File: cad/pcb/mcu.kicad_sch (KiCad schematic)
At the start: 34 parts, among them X4 SWD-Conn, X5 UART_Conn, Y1 32MHz, Y2 32.768k

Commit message: add pcb layout
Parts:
- removed AE1: Antenna_Chip, myLib:Ignion_NN01-102_BT_WIFI, symbol Device:Antenna_Chip
- removed TP10: TXD, TestPoint:TestPoint_Pad_D1.0mm, symbol Connector:TestPoint
- removed TP11: RXD, TestPoint:TestPoint_Pad_D1.0mm, symbol Connector:TestPoint
- removed V6: nRF52810-QFxx, Package_DFN_QFN:QFN-48-1EP_6x6mm_P0.4mm_EP4.6x4.6mm, symbol MCU_Nordic:nRF52810-QFxx
- added AE1: Antenna_Chip, myLib:Ignion_NN01-102_BT_WIFI, symbol Device:Antenna
- added V6: nRF52810-QCxx, Package_DFN_QFN:QFN-32-1EP_5x5mm_P0.5mm_EP3.6x3.6mm, symbol MCU_Nordic:nRF52810-QCxx
- S1: footprint Button_Switch_SMD:SW_SPST_CK_RS282G05A3 -> myLib:Tactile_E-Switch_TL3780AF240QG
- S2, S3: footprint Button_Switch_SMD:SW_SPST_CK_RS282G05A3 -> myLib:Tactile_Panasonic_EVQ-P7J01P
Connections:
- net +3.3V: now also V6.25 (VDD), V6.32 (VDD), V6.9 (VDD)
- net BAT_SENS: now also V6.27 (P0.28/AIN4)
- net BTN0: now also V6.15 (P0.20)
- net BTN1: now also V6.26 (P0.25)
- net CS_IO: now also V6.10 (P0.12)
- net DBG_LED: now also V6.14 (P0.18)
- net DCC: now also V6.31 (DCC)
- net DEC1: now also V6.1 (DEC1)
- net DEC3: now also V6.22 (DEC3)
- net DEC4: now also V6.30 (DEC4)
- net GND: now also V6.20 (VSS), V6.29 (VSS), V6.33 (VSS)
- net GYRO_INT: now also V6.6 (P0.06)
- net HSE1: now also V6.23 (XC1)
- net HSE2: now also V6.24 (XC2)
- net LSE1: now also V6.2 (P0.00/XL1)
- net LSE2: now also V6.3 (P0.01/XL2)
- net MISO: now also V6.13 (P0.16)
- net MOSI: now also V6.11 (P0.14)
- net NRST: now also V6.16 (P0.21/~{RESET})
- net PHOTO: now also V6.28 (P0.30/AIN6)
- net RXD: now also V6.8 (P0.10)
- net SCK: now also V6.12 (P0.15)
- net SCL: now also V6.4 (P0.04/AIN2)
- net SDA: now also V6.5 (P0.05/AIN3)
- net SWDCLK: now also V6.17 (SWDCLK)
- net SWDIO: now also V6.18 (SWDIO)
- net TXD: now also V6.7 (P0.09)
- net ANT_IN: now reaches C17.1, L5.2
- net ANT_IN: now also V6.19 (ANT)
- net RF renamed ANT_TP
- net ANT_TP: now also AE1.1 (A)
- no-connect marks 20 -> 4
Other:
- note removed: "CTS"
- note removed: "RTS"
- moved on the sheet: C14, C8, C9, L3, L4

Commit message: add power section on pcb layout
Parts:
- renumbered C11 to C10, C12 to C11, C13 to C12, C8 to C13, C15 to C14, C9 to C15, C14 to C16, C16 to C17, C17 to C18, C18 to C19, C10 to C9
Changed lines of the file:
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@@
   (symbol (lib_id "power:GND") (at 38.1 190.5 0) (unit 1)
     (in_bom yes) (on_board yes)
-    (property "Reference" "#PWR048" (id 0) (at 38.1 196.85 0)
+    (property "Reference" "#PWR050" (id 0) (at 38.1 196.85 0)
       (effects (font (size 1.27 1.27)) hide)
     )
@@
   (symbol (lib_id "Device:C_Small") (at 101.6 39.37 0) (unit 1)
     (in_bom yes) (on_board yes)
-    (property "Reference" "C11" (id 0) (at 96.52 39.37 0)
+    (property "Reference" "C10" (id 0) (at 96.52 39.37 0)
       (effects (font (size 1.27 1.27)) (justify left))
     )
@@
   (symbol (lib_id "power:GND") (at 233.68 116.84 0) (unit 1)
     (in_bom yes) (on_board yes)
-    (property "Reference" "#PWR041" (id 0) (at 233.68 123.19 0)
+    (property "Reference" "#PWR043" (id 0) (at 233.68 123.19 0)
       (effects (font (size 1.27 1.27)) hide)
     )
@@
   (symbol (lib_id "power:+3.3V") (at 82.55 68.58 0) (unit 1)
     (in_bom yes) (on_board yes)
-    (property "Reference" "#PWR031" (id 0) (at 82.55 72.39 0)
+    (property "Reference" "#PWR037" (id 0) (at 82.55 72.39 0)
       (effects (font (size 1.27 1.27)) hide)
     )
@@
   (symbol (lib_id "power:+3.3V") (at 116.84 33.02 0) (unit 1)
     (in_bom yes) (on_board yes)
-    (property "Reference" "#PWR028" (id 0) (at 116.84 36.83 0)
+    (property "Reference" "#PWR030" (id 0) (at 116.84 36.83 0)
       (effects (font (size 1.27 1.27)) hide)
     )
@@
   (symbol (lib_id "power:+3.3V") (at 130.81 166.37 0) (unit 1)
     (in_bom yes) (on_board yes)
-    (property "Reference" "#PWR046" (id 0) (at 130.81 170.18 0)
+    (property "Reference" "#PWR048" (id 0) (at 130.81 170.18 0)
       (effects (font (size 1.27 1.27)) hide)
     )
@@
   (symbol (lib_id "power:+3.3V") (at 257.81 25.4 0) (unit 1)
     (in_bom yes) (on_board yes)
-    (property "Reference" "#PWR027" (id 0) (at 257.81 29.21 0)
+    (property "Reference" "#PWR029" (id 0) (at 257.81 29.21 0)
       (effects (font (size 1.27 1.27)) hide)
     )
@@
   (symbol (lib_id "power:GND") (at 57.15 68.58 0) (unit 1)
     (in_bom yes) (on_board yes)
-    (property "Reference" "#PWR030" (id 0) (at 57.15 74.93 0)
+    (property "Reference" "#PWR036" (id 0) (at 57.15 74.93 0)
       (effects (font (size 1.27 1.27)) hide)
     )
@@
   (symbol (lib_id "power:GND") (at 233.68 91.44 0) (unit 1)
     (in_bom yes) (on_board yes)
-    (property "Reference" "#PWR038" (id 0) (at 233.68 97.79 0)
+    (property "Reference" "#PWR040" (id 0) (at 233.68 97.79 0)
       (effects (font (size 1.27 1.27)) hide)
     )
@@
   (symbol (lib_id "Device:C_Small") (at 62.23 48.26 270) (unit 1)
     (in_bom yes) (on_board yes)
-    (property "Reference" "C8" (id 0) (at 60.3119 51.0586 90)
+    (property "Reference" "C13" (id 0) (at 60.3119 51.0586 90)
       (effects (font (size 1.27 1.27)) (justify left))
     )
@@
   (symbol (lib_id "Device:C_Small") (at 116.84 39.37 0) (unit 1)
     (in_bom yes) (on_board yes)
-    (property "Reference" "C13" (id 0) (at 111.3214 39.3699 0)
+    (property "Reference" "C12" (id 0) (at 111.3214 39.3699 0)
       (effects (font (size 1.27 1.27)) (justify left))
     )
@@
   (symbol (lib_id "power:GND") (at 130.81 181.61 0) (unit 1)
     (in_bom yes) (on_board yes)
-    (property "Reference" "#PWR047" (id 0) (at 130.81 187.96 0)
+    (property "Reference" "#PWR049" (id 0) (at 130.81 187.96 0)
       (effects (font (size 1.27 1.27)) hide)
     )
@@
   (symbol (lib_id "power:GND") (at 54.61 86.36 0) (unit 1)
     (in_bom yes) (on_board yes)
-    (property "Reference" "#PWR037" (id 0) (at 54.61 92.71 0)
+    (property "Reference" "#PWR039" (id 0) (at 54.61 92.71 0)
       (effects (font (size 1.27 1.27)) hide)
     )
@@
   (symbol (lib_id "Device:C_Small") (at 194.31 38.1 270) (mirror x) (unit 1)
     (in_bom yes) (on_board yes)
-    (property "Reference" "C10" (id 0) (at 194.3257 41.055 90))
+    (property "Reference" "C9" (id 0) (at 194.3257 41.055 90))
     (property "Value" "12p" (id 1) (at 194.2453 42.8228 90))
     (property "Footprint" "Capacitor_SMD:C_0603_1608Metric" (id 2) (at 194.31 38.1 0)
@@
   (symbol (lib_id "power:GND") (at 116.84 45.72 0) (unit 1)
     (in_bom yes) (on_board yes)
-    (property "Reference" "#PWR029" (id 0) (at 116.84 52.07 0)
+    (property "Reference" "#PWR031" (id 0) (at 116.84 52.07 0)
       (effects (font (size 1.27 1.27)) hide)
     )
@@
   (symbol (lib_id "power:+3.3V") (at 40.64 152.4 0) (unit 1)
     (in_bom yes) (on_board yes)
-    (property "Reference" "#PWR045" (id 0) (at 40.64 156.21 0)
+    (property "Reference" "#PWR047" (id 0) (at 40.64 156.21 0)
       (effects (font (size 1.27 1.27)) hide)
     )
@@
   (symbol (lib_id "Device:C_Small") (at 109.22 39.37 0) (unit 1)
     (in_bom yes) (on_board yes)
-    (property "Reference" "C12" (id 0) (at 104.14 39.37 0)
+    (property "Reference" "C11" (id 0) (at 104.14 39.37 0)
       (effects (font (size 1.27 1.27)) (justify left))
     )
@@
   (symbol (lib_id "power:+3.3V") (at 251.46 77.47 0) (unit 1)
     (in_bom yes) (on_board yes)
-    (property "Reference" "#PWR036" (id 0) (at 251.46 81.28 0)
+    (property "Reference" "#PWR038" (id 0) (at 251.46 81.28 0)
       (effects (font (size 1.27 1.27)) hide)
     )
@@
   (symbol (lib_id "Device:C_Small") (at 62.23 55.88 270) (unit 1)
     (in_bom yes) (on_board yes)
-    (property "Reference" "C9" (id 0) (at 60.277 58.6466 90)
+    (property "Reference" "C15" (id 0) (at 60.277 58.6466 90)
       (effects (font (size 1.27 1.27)) (justify left))
     )
@@
   (symbol (lib_id "Device:C_Small") (at 194.31 88.9 270) (mirror x) (unit 1)
     (in_bom yes) (on_board yes)
-    (property "Reference" "C18" (id 0) (at 194.4037 91.681 90))
+    (property "Reference" "C19" (id 0) (at 194.4037 91.681 90))
     (property "Value" "12p" (id 1) (at 194.2832 93.4889 90))
     (property "Footprint" "Capacitor_SMD:C_0603_1608Metric" (id 2) (at 194.31 88.9 0)
@@
   (symbol (lib_id "Device:C_Small") (at 62.23 63.5 270) (unit 1)
     (in_bom yes) (on_board yes)
-    (property "Reference" "C14" (id 0) (at 60.277 66.5142 90)
+    (property "Reference" "C16" (id 0) (at 60.277 66.5142 90)
       (effects (font (size 1.27 1.27)) (justify left))
     )
@@
   (symbol (lib_id "power:+3.3V") (at 251.46 128.27 0) (unit 1)
     (in_bom yes) (on_board yes)
-    (property "Reference" "#PWR042" (id 0) (at 251.46 132.08 0)
+    (property "Reference" "#PWR045" (id 0) (at 251.46 132.08 0)
       (effects (font (size 1.27 1.27)) hide)
     )
@@
   (symbol (lib_id "Device:C_Small") (at 194.31 50.8 270) (mirror x) (unit 1)
     (in_bom yes) (on_board yes)
-    (property "Reference" "C15" (id 0) (at 194.4037 53.581 90))
+    (property "Reference" "C14" (id 0) (at 194.4037 53.581 90))
     (property "Value" "12p" (id 1) (at 194.2832 55.3889 90))
     (property "Footprint" "Capacitor_SMD:C_0603_1608Metric" (id 2) (at 194.31 50.8 0)
@@
   (symbol (lib_id "power:GND") (at 203.2 92.71 0) (mirror y) (unit 1)
     (in_bom yes) (on_board yes)
-    (property "Reference" "#PWR039" (id 0) (at 203.2 99.06 0)
+    (property "Reference" "#PWR041" (id 0) (at 203.2 99.06 0)
       (effects (font (size 1.27 1.27)) hide)
     )
@@
   (symbol (lib_id "Device:C_Small") (at 194.31 76.2 270) (mirror x) (unit 1)
     (in_bom yes) (on_board yes)
-    (property "Reference" "C16" (id 0) (at 194.3257 79.155 90))
+    (property "Reference" "C17" (id 0) (at 194.3257 79.155 90))
     (property "Value" "12p" (id 1) (at 194.2453 80.9228 90))
     (property "Footprint" "Capacitor_SMD:C_0603_1608Metric" (id 2) (at 194.31 76.2 0)
@@
   (symbol (lib_id "Device:C_Small") (at 54.61 82.55 0) (unit 1)
     (in_bom yes) (on_board yes)
-    (property "Reference" "C17" (id 0) (at 48.9952 82.5703 0)
+    (property "Reference" "C18" (id 0) (at 48.9952 82.5703 0)
       (effects (font (size 1.27 1.27)) (justify left))
     )
@@
   (symbol (lib_id "power:GND") (at 177.8 139.7 0) (unit 1)
     (in_bom yes) (on_board yes)
-    (property "Reference" "#PWR043" (id 0) (at 177.8 146.05 0)
+    (property "Reference" "#PWR046" (id 0) (at 177.8 146.05 0)
       (effects (font (size 1.27 1.27)) hide)
     )
@@
   (symbol (lib_id "power:+3.3V") (at 251.46 102.87 0) (unit 1)
     (in_bom yes) (on_board yes)
-    (property "Reference" "#PWR040" (id 0) (at 251.46 106.68 0)
+    (property "Reference" "#PWR042" (id 0) (at 251.46 106.68 0)
       (effects (font (size 1.27 1.27)) hide)
     )
@@
   (symbol (lib_id "power:+3.3V") (at 245.11 25.4 0) (unit 1)
     (in_bom yes) (on_board yes)
-    (property "Reference" "#PWR026" (id 0) (at 245.11 29.21 0)
-      (effects (font (size 1.27 1.27)) hide)
-    )
+    (property "Reference" "#PWR028" (id 0) (at 245.11 29.21 0)
+      (effects (font (size 1.27 1.27)) hide)
+    )

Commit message: add back layer led-ring
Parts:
- S2, S3: footprint myLib:Tactile_Panasonic_EVQ-P7J01P -> myLib:Tactile_Panasonic_EVQP7J01P
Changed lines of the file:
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@@
     (property "Reference" "S2" (id 0) (at 242.57 92.71 0))
     (property "Value" "BTN0" (id 1) (at 242.57 95.25 0))
-    (property "Footprint" "myLib:Tactile_Panasonic_EVQ-P7J01P" (id 2) (at 242.57 88.9 0)
+    (property "Footprint" "myLib:Tactile_Panasonic_EVQP7J01P" (id 2) (at 242.57 88.9 0)
       (effects (font (size 1.27 1.27)) hide)
     )
@@
     (property "Reference" "S3" (id 0) (at 242.57 118.11 0))
     (property "Value" "BTN1" (id 1) (at 242.57 120.65 0))
-    (property "Footprint" "myLib:Tactile_Panasonic_EVQ-P7J01P" (id 2) (at 242.57 114.3 0)
+    (property "Footprint" "myLib:Tactile_Panasonic_EVQP7J01P" (id 2) (at 242.57 114.3 0)
       (effects (font (size 1.27 1.27)) hide)
     )

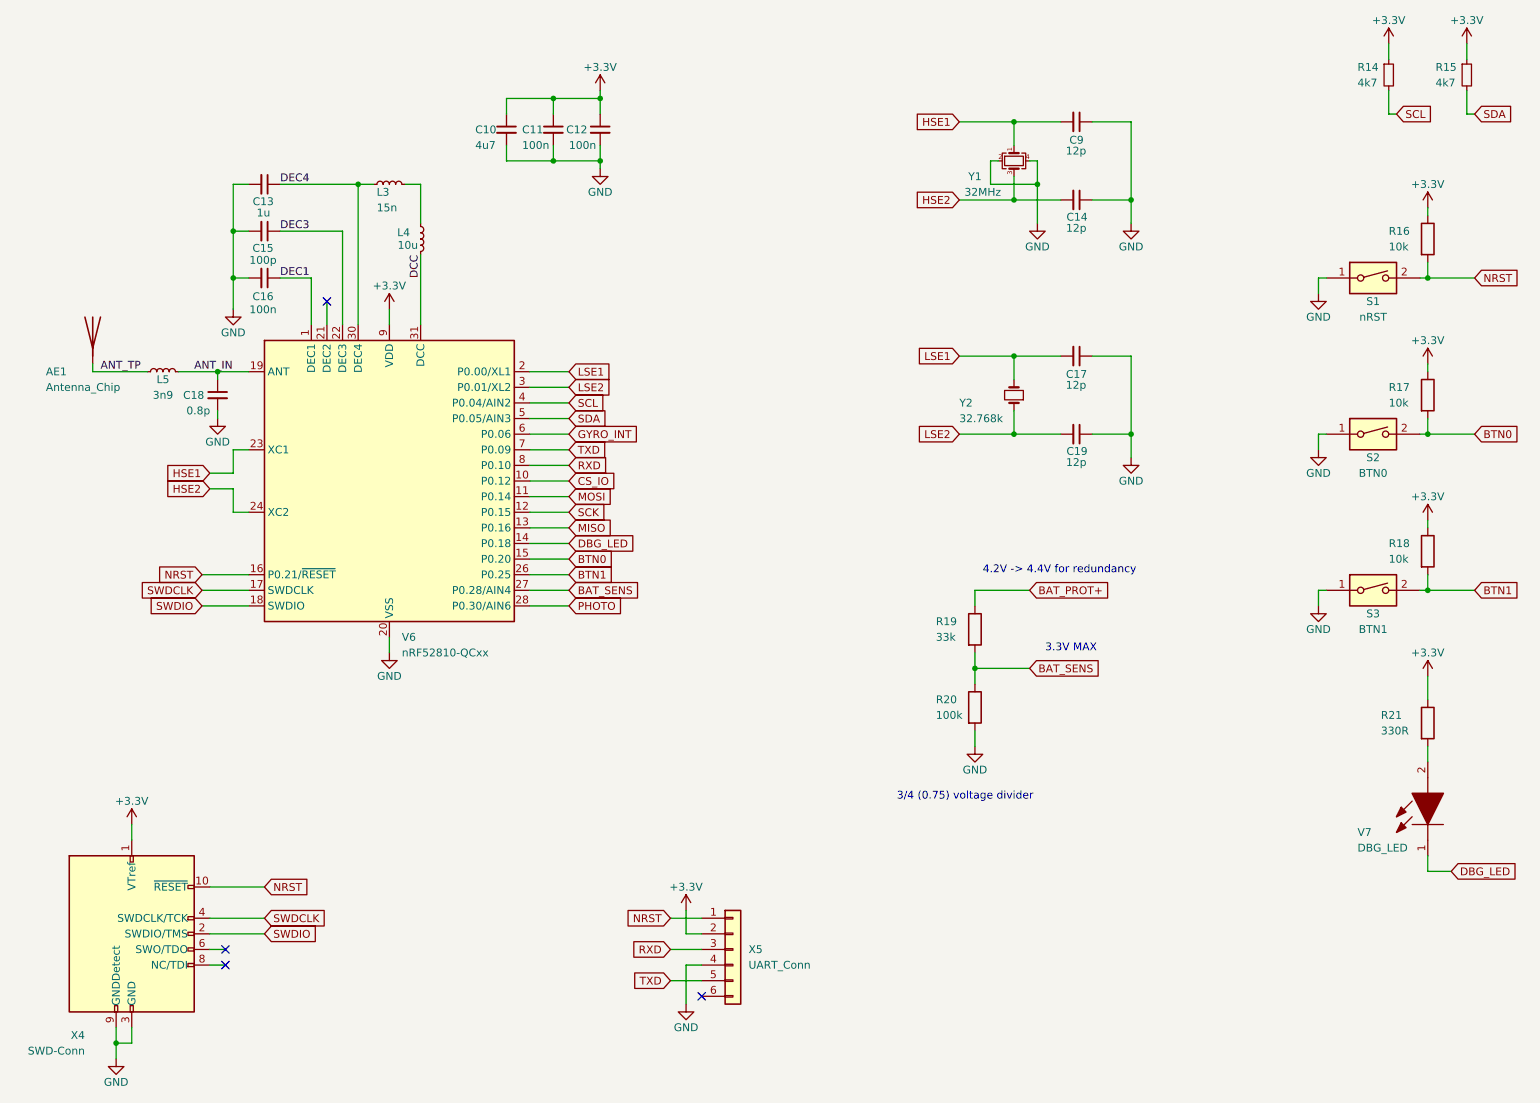
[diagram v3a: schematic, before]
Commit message: add 3d models for pcb layout
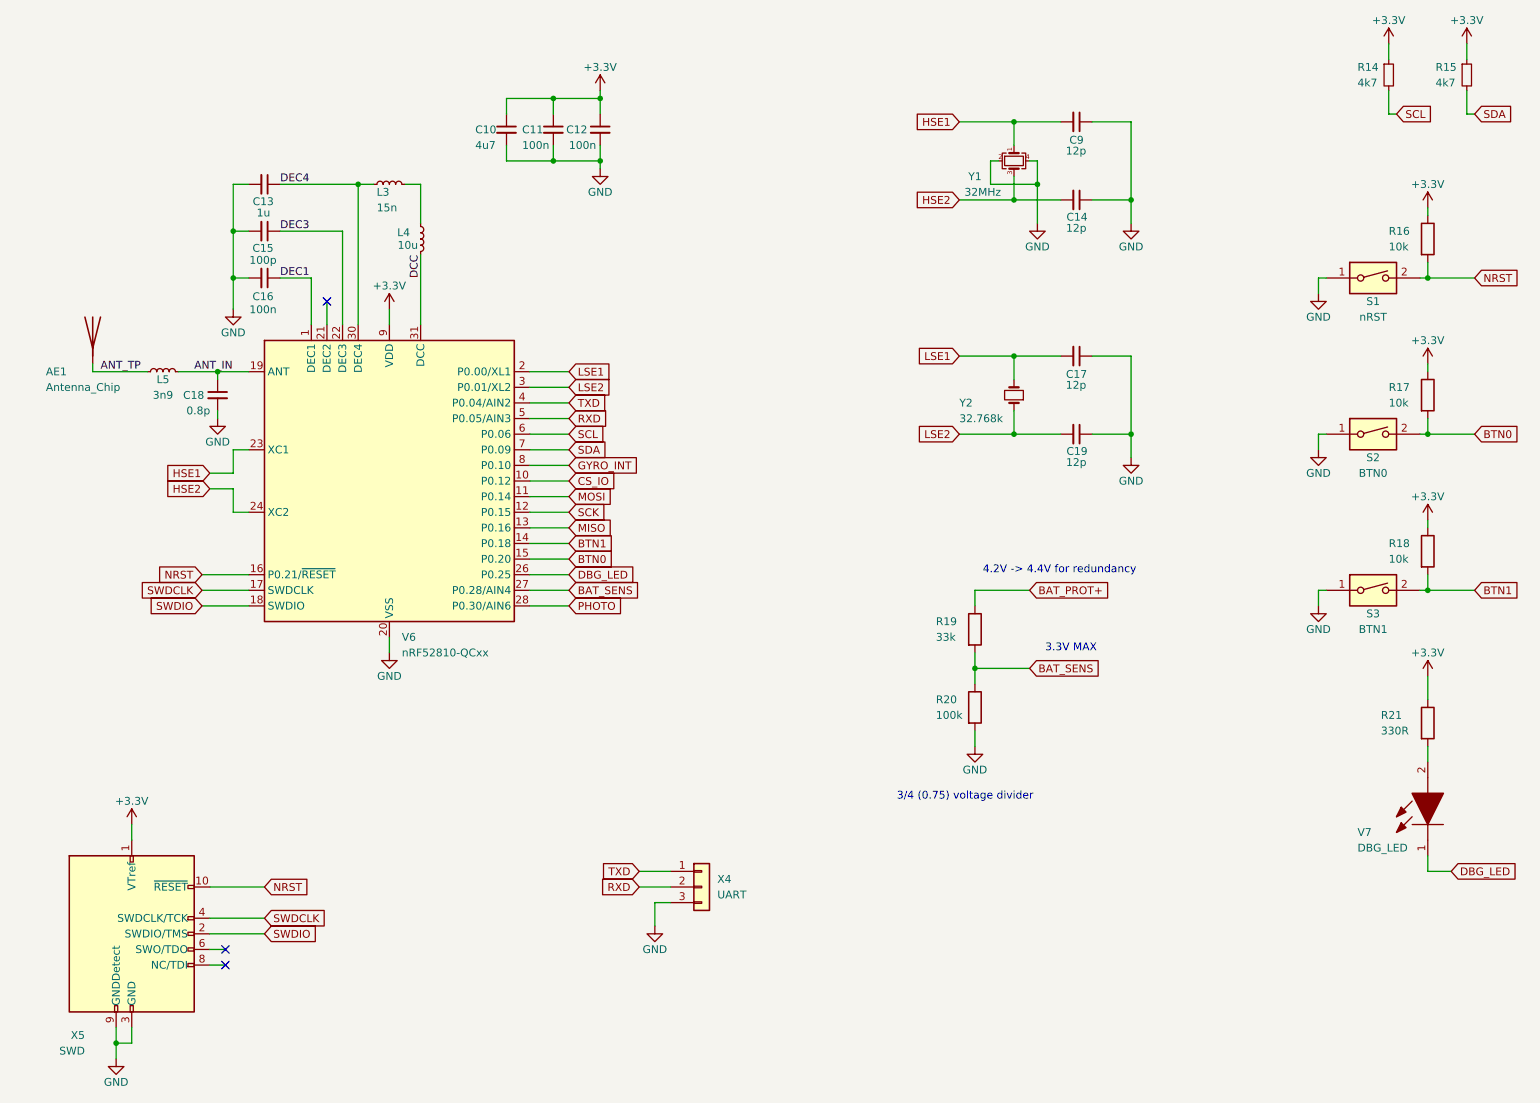
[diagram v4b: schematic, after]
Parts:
- removed X5: UART_Conn, Connector_PinHeader_1.27mm:PinHeader_2x03_P1.27mm_Vertical_SMD, symbol Connector_Generic:Conn_01x06
- added X4: UART, myLib:PinHeader_P2mm_1x03_SMD, symbol Connector_Generic:Conn_01x03
- X5: renamed from X4; value SWD-Conn -> SWD; footprint Connector_PinHeader_1.27mm:PinHeader_2x05_P1.27mm_Vertical_SMD -> myLib:PinHeader_2x05_P1.27mm_Vertical_SMD
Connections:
- net BTN1: now also V6.14 (P0.18); no longer V6.26 (P0.25)
- net DBG_LED: now also V6.26 (P0.25); no longer V6.14 (P0.18)
- net GND: now also X4.3 (Pin_3)
- net GYRO_INT: now also V6.8 (P0.10); no longer V6.6 (P0.06)
- net RXD: now also V6.5 (P0.05/AIN3), X4.2 (Pin_2); no longer V6.8 (P0.10)
- net SCL: now also V6.6 (P0.06); no longer V6.4 (P0.04/AIN2)
- net SDA: now also V6.7 (P0.09); no longer V6.5 (P0.05/AIN3)
- net TXD: now also V6.4 (P0.04/AIN2), X4.1 (Pin_1); no longer V6.7 (P0.09)
- no-connect marks 4 -> 3
